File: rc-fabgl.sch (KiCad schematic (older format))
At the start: 44 parts, among them J1 RC2014, J2 RC2014_Enh, J3 Serial, J5 Keyboard, J6 VGA, Q1 2N7000, Q2 2N7000, SW1 Reset, SW2 Boot, U1 MCP1825S, U2 ESP32-WROVER-E, U3 74LVC125

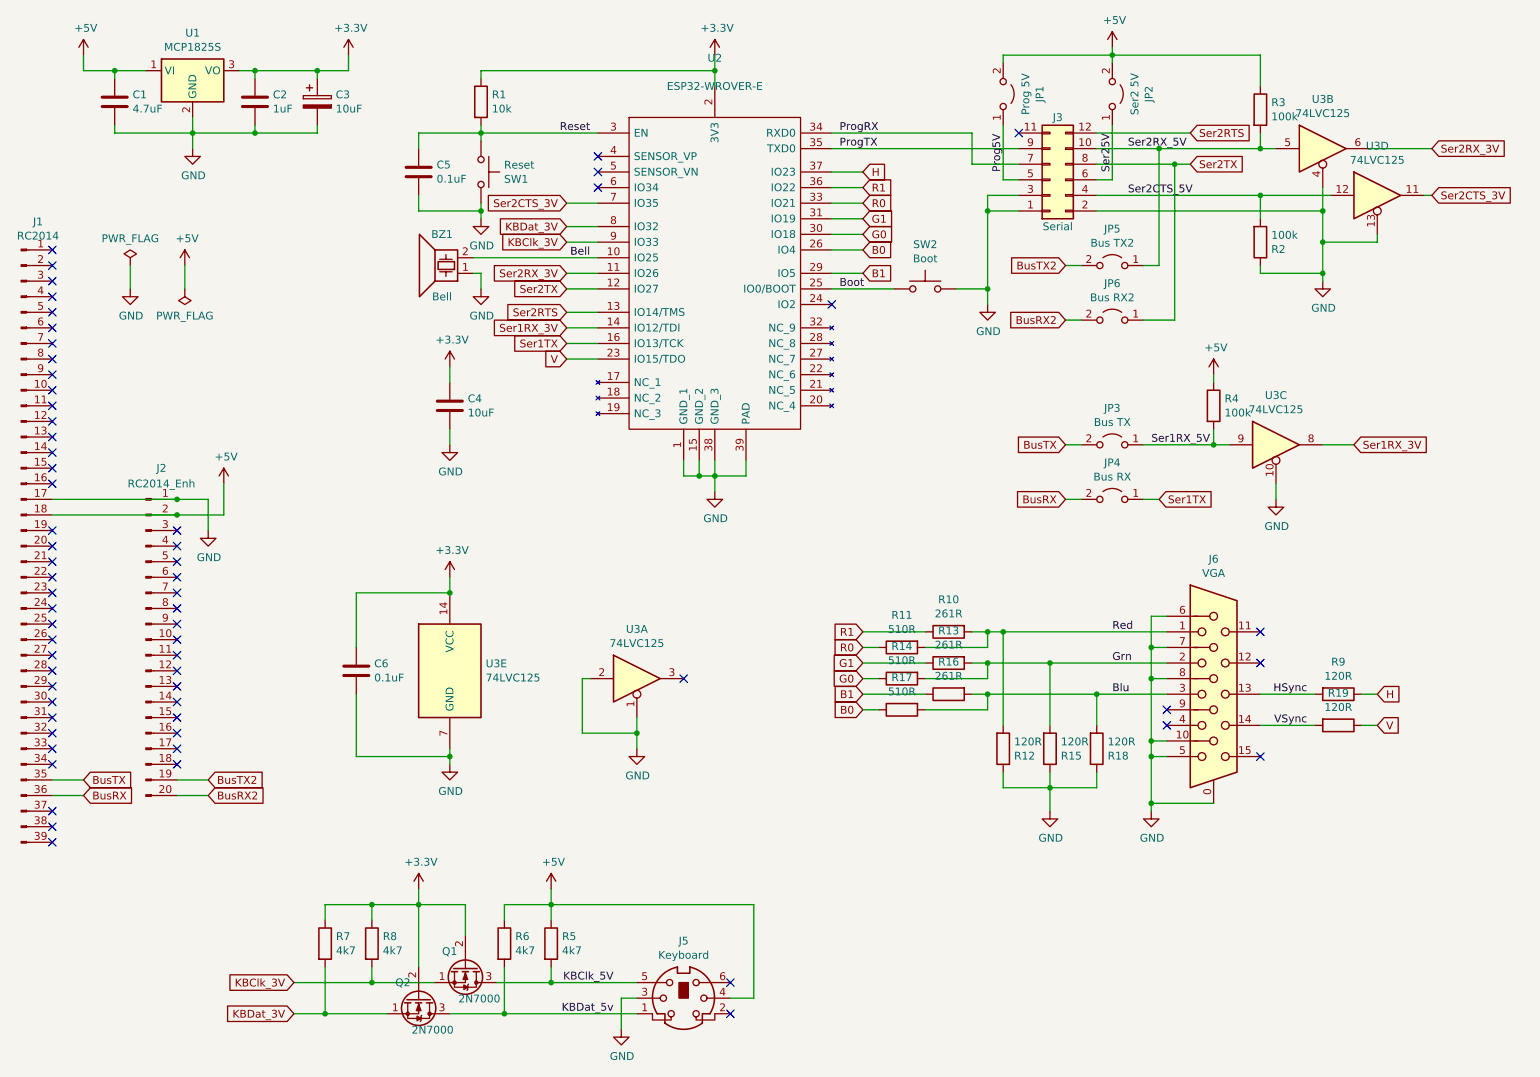
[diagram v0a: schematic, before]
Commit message: Fixed component references, footprint 3D paths
Fixed component references, and corrected footprint 3D model paths. Changed serial headers to single right-angle part.
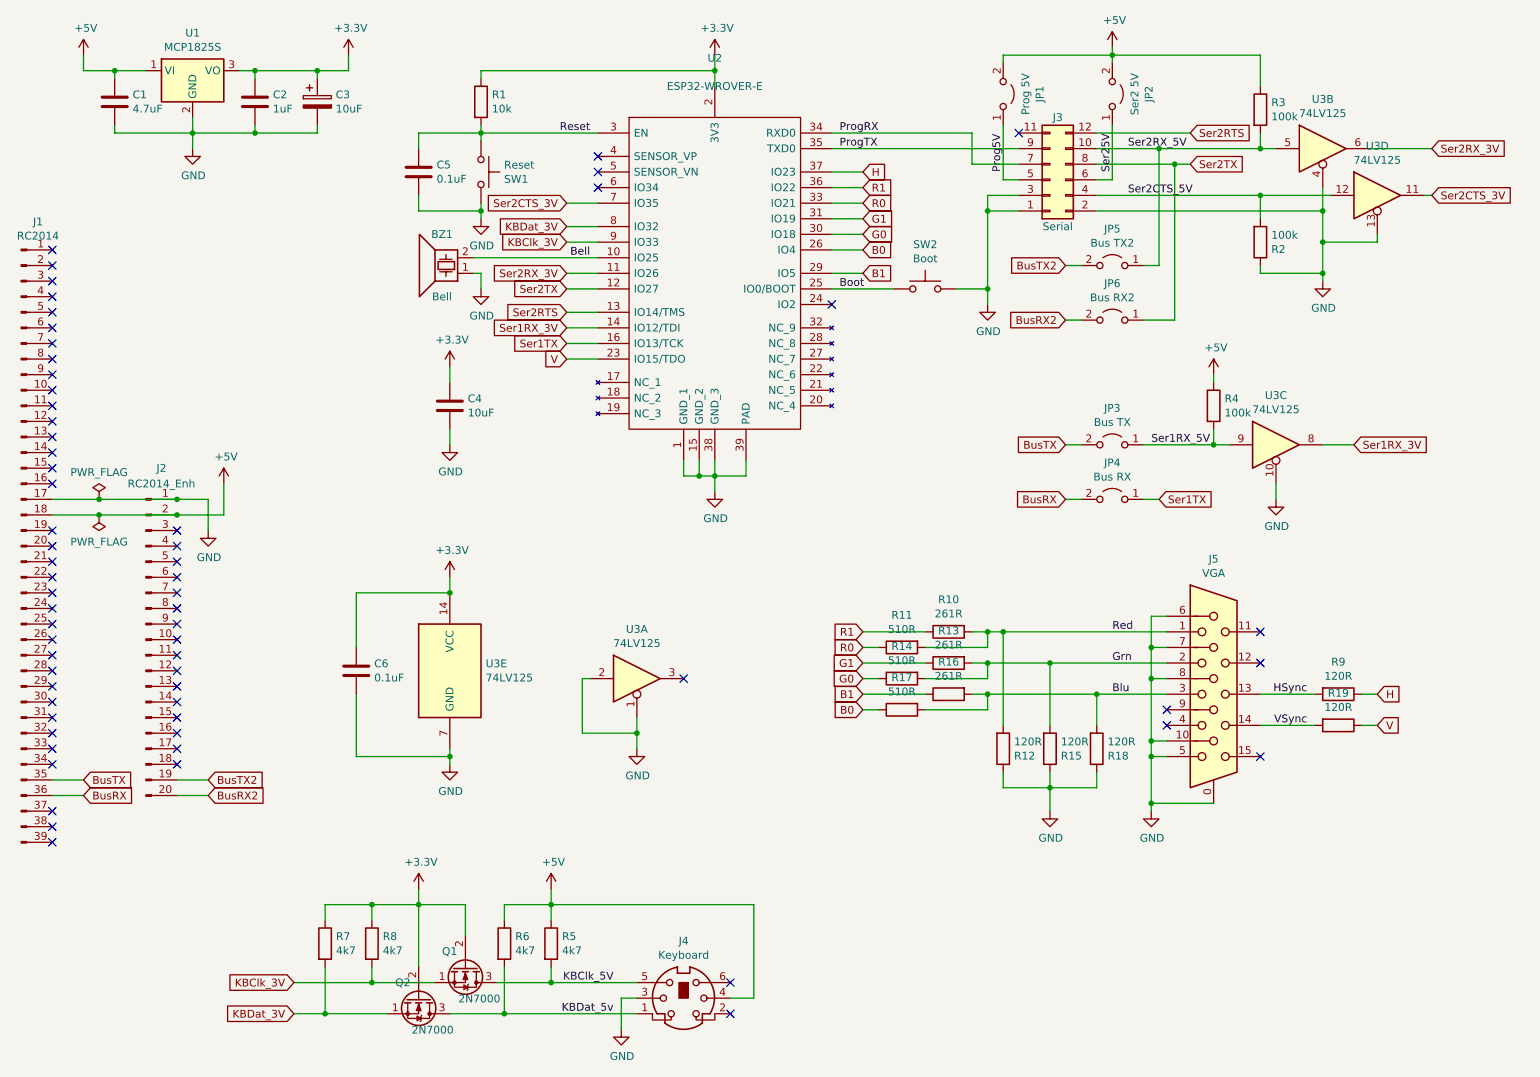
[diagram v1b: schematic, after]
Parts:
- U3: value 74LVC125 -> 74LV125
- renumbered J5 to J4, J6 to J5
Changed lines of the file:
@@
 L power:PWR_FLAG #FLG0101
 U 1 1 5F38A23A
-P 1450 2300
-F 0 "#FLG0101" H 1450 2375 50  0001 C CNN
-F 1 "PWR_FLAG" H 1450 2473 50  0000 C CNN
-F 2 "" H 1450 2300 50  0001 C CNN
-F 3 "~" H 1450 2300 50  0001 C CNN
-	1    1450 2300
+P 1250 3800
+F 0 "#FLG0101" H 1250 3875 50  0001 C CNN
+F 1 "PWR_FLAG" H 1250 3973 50  0000 C CNN
+F 2 "" H 1250 3800 50  0001 C CNN
+F 3 "~" H 1250 3800 50  0001 C CNN
+	1    1250 3800
 	1    0    0    -1
 $EndComp
@@
 L power:PWR_FLAG #FLG0102
 U 1 1 5F38B194
-P 1800 2450
-F 0 "#FLG0102" H 1800 2525 50  0001 C CNN
-F 1 "PWR_FLAG" H 1800 2623 50  0000 C CNN
-F 2 "" H 1800 2450 50  0001 C CNN
-F 3 "~" H 1800 2450 50  0001 C CNN
-	1    1800 2450
+P 1250 3900
+F 0 "#FLG0102" H 1250 3975 50  0001 C CNN
+F 1 "PWR_FLAG" H 1250 4073 50  0000 C CNN
+F 2 "" H 1250 3900 50  0001 C CNN
+F 3 "~" H 1250 3900 50  0001 C CNN
+	1    1250 3900
 	-1   0    0    1
 $EndComp
-$Comp
-L power:GND #PWR0116
-U 1 1 5F38B9CE
-P 1450 2450
-F 0 "#PWR0116" H 1450 2200 50  0001 C CNN
-F 1 "GND" H 1455 2277 50  0000 C CNN
-F 2 "" H 1450 2450 50  0001 C CNN
-F 3 "" H 1450 2450 50  0001 C CNN
-	1    1450 2450
-	1    0    0    -1
-$EndComp
-$Comp
-L power:+5V #PWR0117
-U 1 1 5F38BE5F
-P 1800 2300
-F 0 "#PWR0117" H 1800 2150 50  0001 C CNN
-F 1 "+5V" H 1815 2473 50  0000 C CNN
-F 2 "" H 1800 2300 50  0001 C CNN
-F 3 "" H 1800 2300 50  0001 C CNN
-	1    1800 2300
-	1    0    0    -1
-$EndComp
-Wire Wire Line
-	1450 2300 1450 2450
-Wire Wire Line
-	1800 2300 1800 2450
 $Comp
 L power:GND #PWR0102
@@
 	2050 3900 1750 3900
 Wire Wire Line
-	950  3900 1750 3900
+	950  3900 1250 3900
 Connection ~ 1750 3900
 Wire Wire Line
@@
 	1950 3800 1950 4000
 Wire Wire Line
-	950  3800 1750 3800
+	950  3800 1250 3800
 Connection ~ 1750 3800
 NoConn ~ 1750 4000
@@
 $EndComp
 $Comp
-L Connector:Mini-DIN-6 J5
+L Connector:Mini-DIN-6 J4
 U 1 1 5FB2CDA8
 P 5000 7000
-F 0 "J5" H 5000 7367 50  0000 C CNN
+F 0 "J4" H 5000 7367 50  0000 C CNN
 F 1 "Keyboard" H 5000 7276 50  0000 C CNN
 F 2 "rc-fabgl:Mini-DIN-6-Socket" H 5000 7000 50  0001 C CNN
@@
 $EndComp
 $Comp
-L Connector:DB15_Female_HighDensity_MountingHoles J6
+L Connector:DB15_Female_HighDensity_MountingHoles J5
 U 1 1 5FCB1A2F
 P 8400 5050
-F 0 "J6" H 8400 5917 50  0000 C CNN
+F 0 "J5" H 8400 5917 50  0000 C CNN
 F 1 "VGA" H 8400 5826 50  0000 C CNN
 F 2 "rc-fabgl:DSUB-15-HD_Female_Horizontal_P2.29x2.54mm_Housed" H 7450 5450 50  0001 C CNN
@@
 P 4700 4950
 F 0 "U3" H 4700 5267 50  0000 C CNN
-F 1 "74LVC125" H 4700 5176 50  0000 C CNN
+F 1 "74LV125" H 4700 5176 50  0000 C CNN
 F 2 "Package_DIP:DIP-14_W7.62mm_LongPads" H 4700 4950 50  0001 C CNN
 F 3 "http://www.ti.com/lit/gpn/sn74LVC125" H 4700 4950 50  0001 C CNN
@@
 P 8800 3450
 F 0 "U3" H 8800 3767 50  0000 C CNN
-F 1 "74LVC125" H 8800 3676 50  0000 C CNN
+F 1 "74LV125" H 8800 3676 50  0000 C CNN
 F 2 "Package_DIP:DIP-14_W7.62mm_LongPads" H 8800 3450 50  0001 C CNN
 F 3 "http://www.ti.com/lit/gpn/sn74LVC125" H 8800 3450 50  0001 C CNN
@@
 P 3500 4900
 F 0 "U3" H 3730 4946 50  0000 L CNN
-F 1 "74LVC125" H 3730 4855 50  0000 L CNN
+F 1 "74LV125" H 3730 4855 50  0000 L CNN
 F 2 "Package_DIP:DIP-14_W7.62mm_LongPads" H 3500 4900 50  0001 C CNN
 F 3 "http://www.ti.com/lit/gpn/sn74LVC125" H 3500 4900 50  0001 C CNN
@@
 P 9100 1550
 F 0 "U3" H 9100 1867 50  0000 C CNN
-F 1 "74LVC125" H 9100 1776 50  0000 C CNN
+F 1 "74LV125" H 9100 1776 50  0000 C CNN
 F 2 "Package_DIP:DIP-14_W7.62mm_LongPads" H 9100 1550 50  0001 C CNN
 F 3 "http://www.ti.com/lit/gpn/sn74LVC125" H 9100 1550 50  0001 C CNN
@@
 P 9450 1850
 F 0 "U3" H 9450 2167 50  0000 C CNN
-F 1 "74LVC125" H 9450 2076 50  0000 C CNN
+F 1 "74LV125" H 9450 2076 50  0000 C CNN
 F 2 "Package_DIP:DIP-14_W7.62mm_LongPads" H 9450 1850 50  0001 C CNN
 F 3 "http://www.ti.com/lit/gpn/sn74LVC125" H 9450 1850 50  0001 C CNN
@@
 Wire Wire Line
 	3300 6300 3300 6400
+Connection ~ 1250 3800
+Wire Wire Line
+	1250 3800 1750 3800
+Connection ~ 1250 3900
+Wire Wire Line
+	1250 3900 1750 3900
 $EndSCHEMATC

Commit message: Fix strapping pin issue - isolate Ser1 during reset
Used spare buffer to invert and delay reset signal, used that to disable Ser1 during reset. This prevents GPIO12 from setting the flash/PSRAM voltage incorrectly. Keyboard footprint was reversed (thanks for nothing SamacSys!)
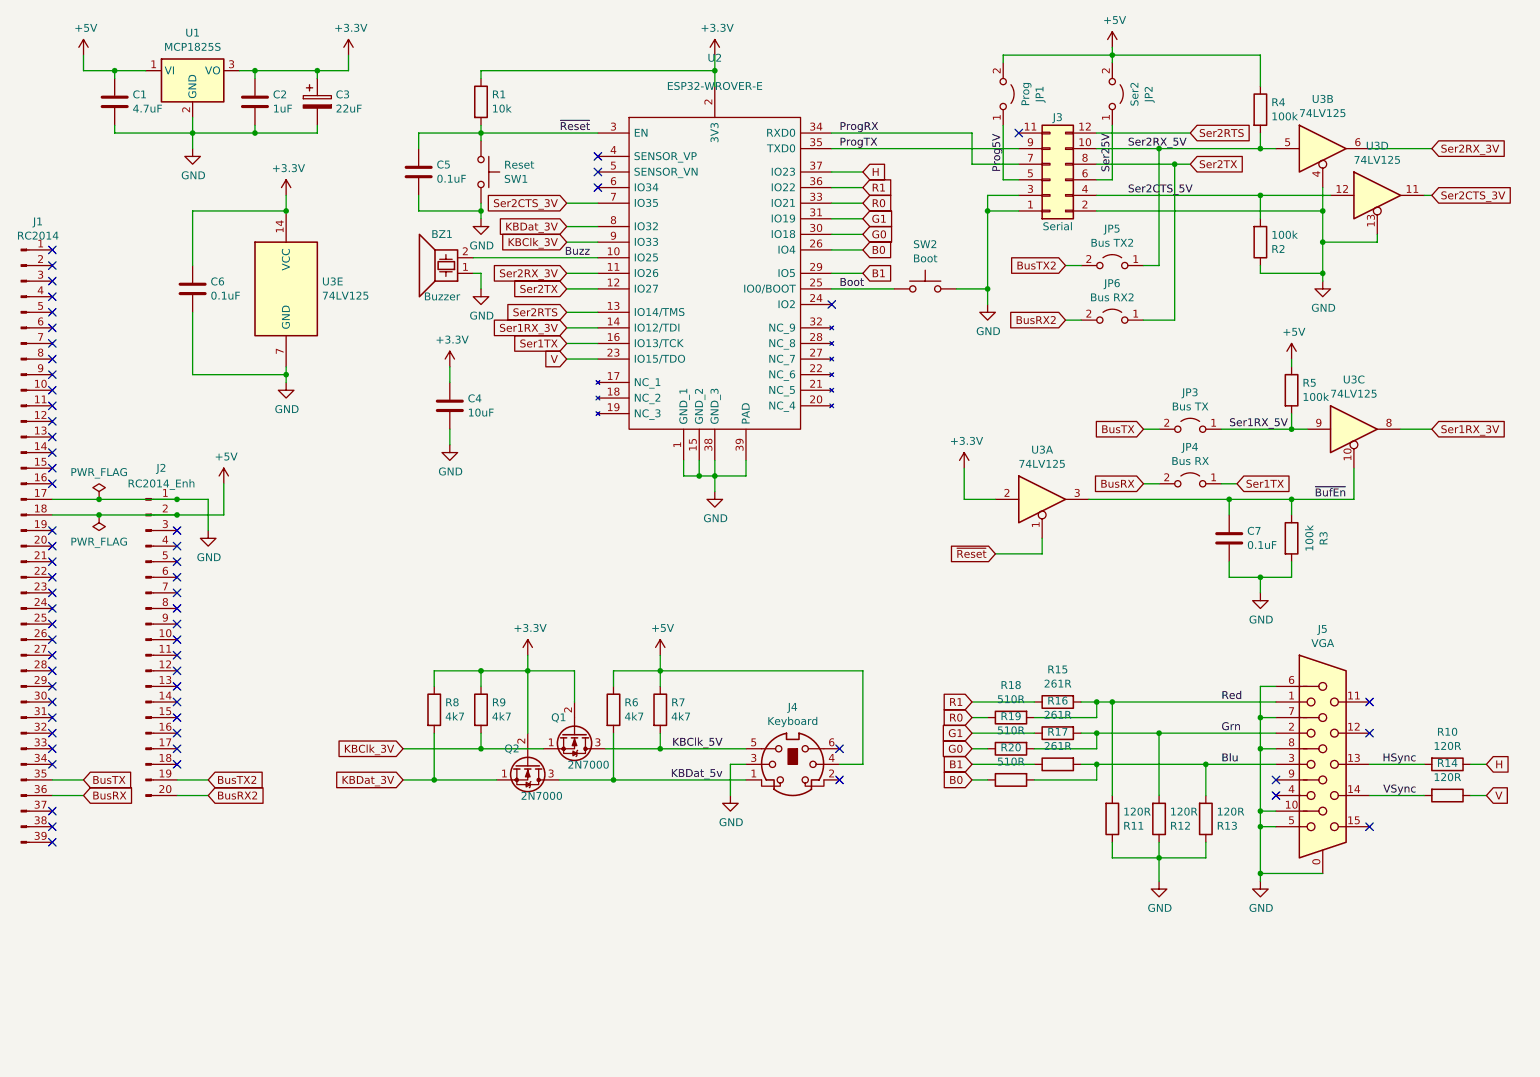
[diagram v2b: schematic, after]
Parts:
- added C7: 0.1uF, Capacitor_THT:C_Disc_D3.0mm_W1.6mm_P2.50mm, symbol Device:C
- added R3: 100k, Resistor_THT:R_Axial_DIN0207_L6.3mm_D2.5mm_P7.62mm_Horizontal, symbol Device:R
- BZ1: value Bell -> Buzzer
- C3: value 10uF -> 22uF
- JP1: value Prog 5V -> Prog
- JP2: value Ser2 5V -> Ser2
- renumbered R9 to R10, R12 to R11, R15 to R12, R18 to R13, R19 to R14, R10 to R15, R13 to R16, R16 to R17, R11 to R18, R14 to R19, R17 to R20, R3 to R4, R4 to R5, R5 to R7, R7 to R8, R8 to R9
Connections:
- net +3V3: now also U3.2
- net GND: now also C7.1, R3.2; no longer U3.1, U3.10, U3.2
- net ~BufEn: now reaches U3.3
- net ~BufEn: now also U3.10, C7.2, R3.1
- net Bell renamed Buzz
- net Reset renamed ~Reset
- net ~Reset: now also U3.1
- no-connect marks 64 -> 63
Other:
- moved on the sheet: C6, J4, J5, JP3, JP4, Q1, Q2, R10, R11, R12, R13, R14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
